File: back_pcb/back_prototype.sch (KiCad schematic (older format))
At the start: 89 parts, among them P1 EXPANSION_LEFT, P2 EXPANSION_BOTTOM, P3 EXPANSION_TOP, P4 USB_A, P5 CONN_01X04, P6 ATMEGA_HEADER, P7 EXPANSION_BOTTOM2, P8 CONN_01X02, Q1 Q_PMOS_GSD, Q2 Q_NMOS_GSD, Q3 Q_NMOS_GSD, U1 PI ZERO, U2 SIM800_BREAKOUT, U3 MCP23017, U4 TP4056_BREAKOUT, U5 RTC, Y1 Crystal_Small

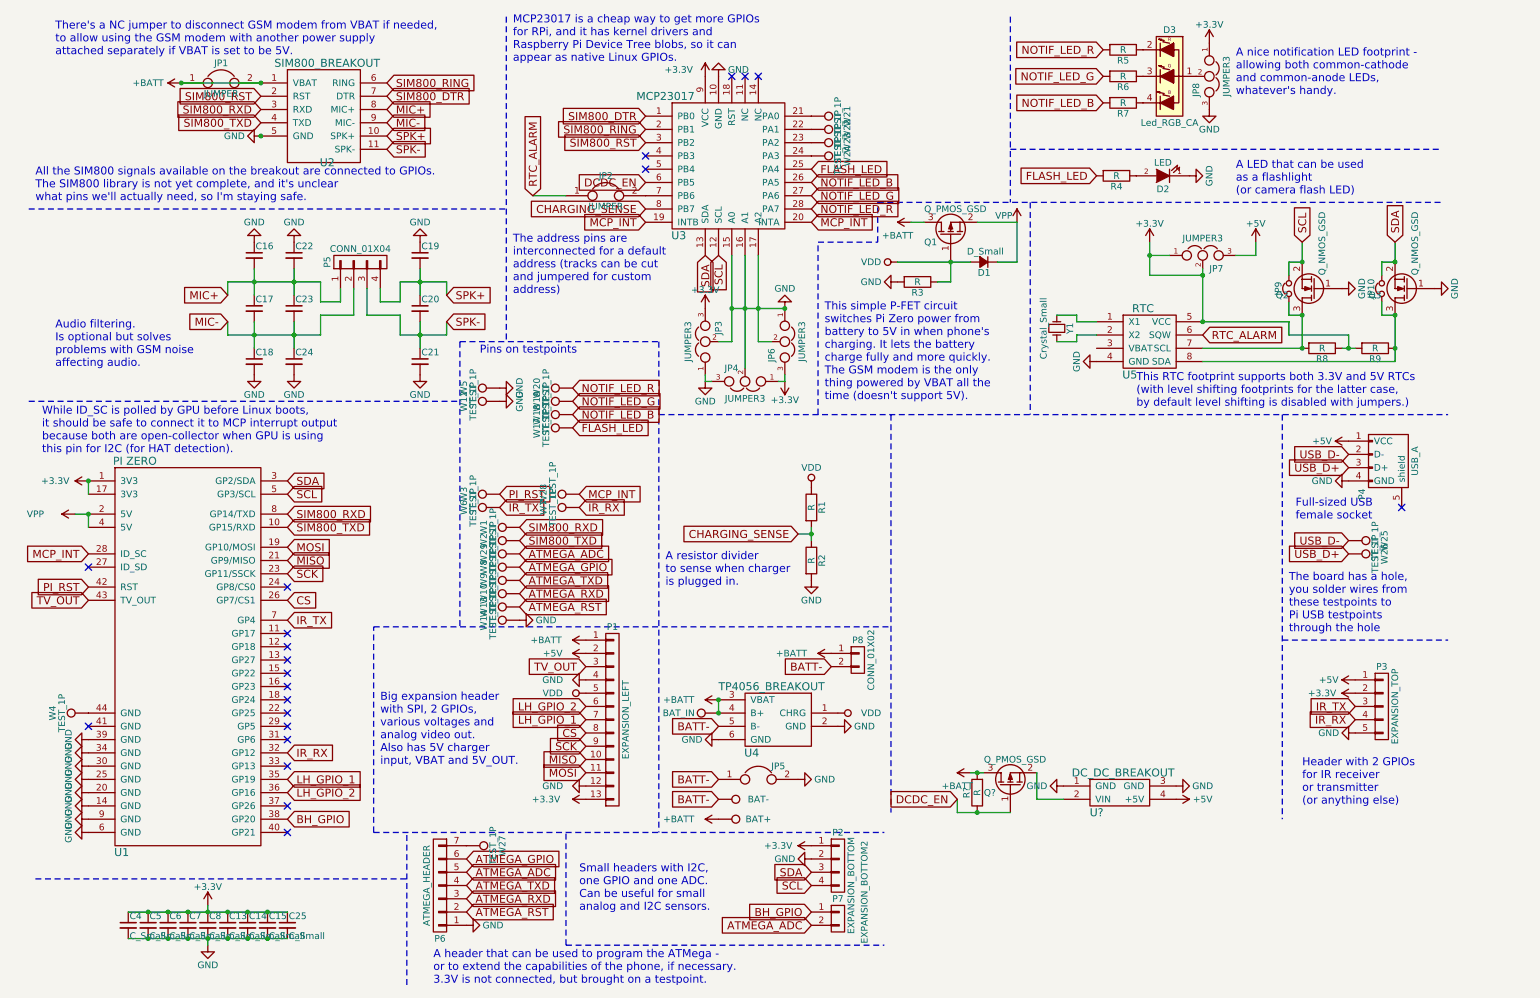
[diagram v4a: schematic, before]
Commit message: Back board finished - untested, not pretty
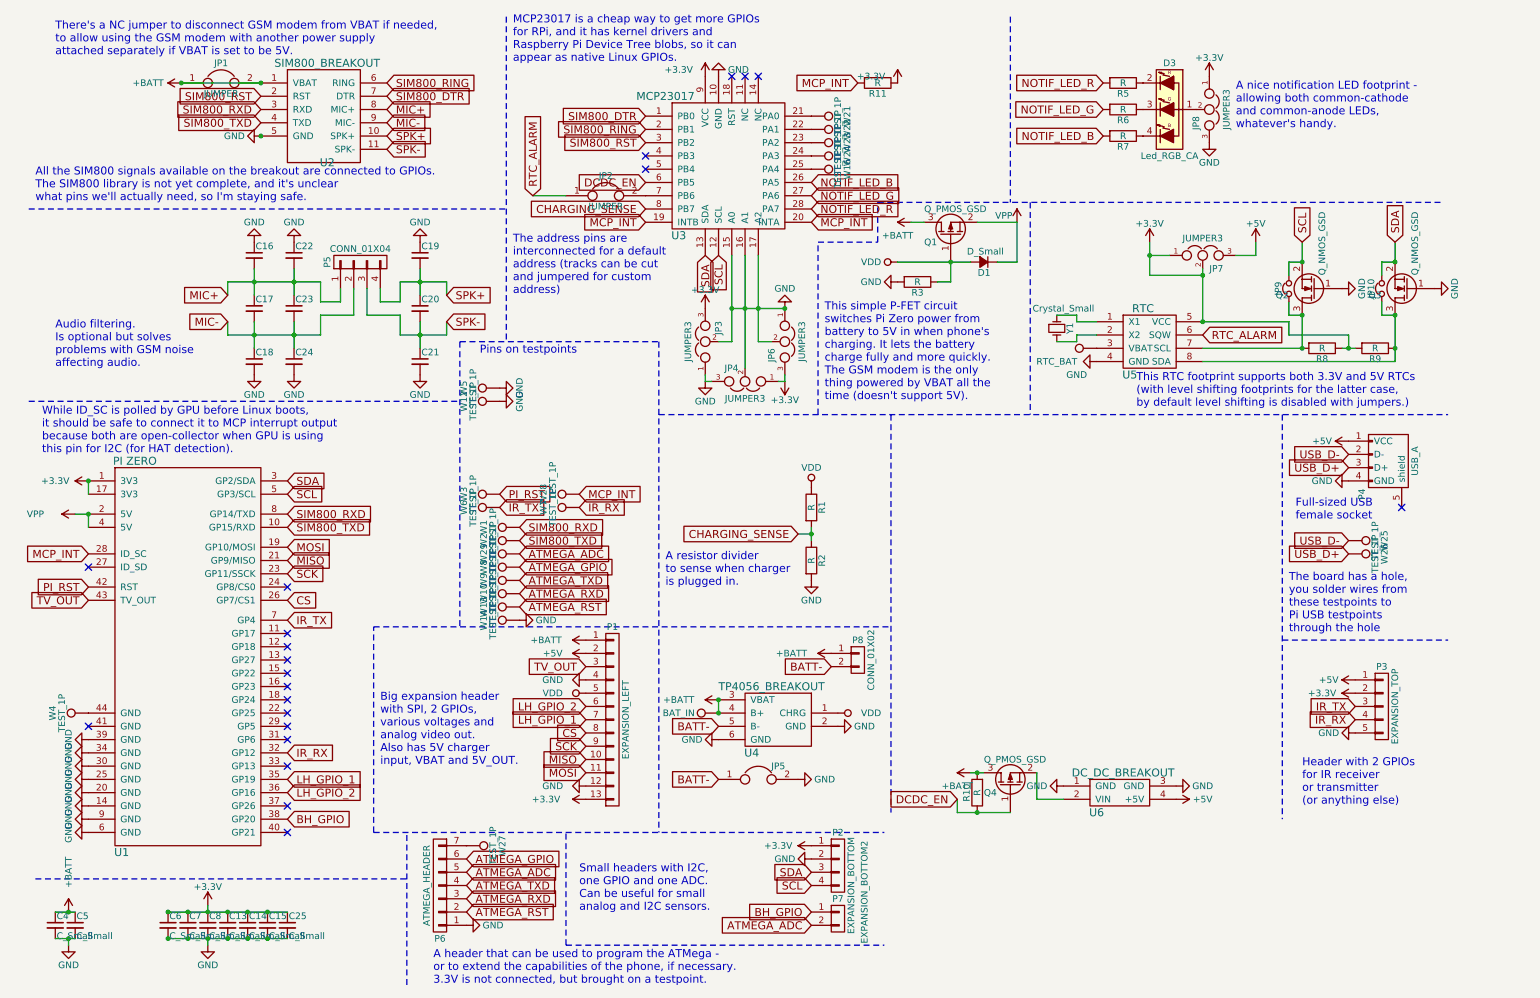
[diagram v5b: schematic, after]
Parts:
- removed D2: LED, symbol LED
- removed R4: R, Resistors_SMD:R_0805_HandSoldering, symbol R
- removed W17, W18, W19, W20: TEST_1P, Measurement_Points:Measurement_Point_Square-SMD-Pad_Small, symbol TEST_1P
- added R11: R, Resistors_SMD:R_0805_HandSoldering, symbol R
- C4: footprint Capacitors_SMD:C_0805 -> Capacitors_Tantalum_SMD:CP_Tantalum_Case-B_EIA-3528-21_Hand
- D3: footprint (none) -> footprints:RGB_5050
- U6: renamed from U?; footprint (none) -> footprints:DC-DC-BREAKOUT
- W15: value BAT- -> RTC_BAT
- W16: value BAT+ -> TEST_1P
- gave numbers to parts that had none: 2
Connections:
- net +3V3: now also R11.1; no longer C4.1, C5.1
- net +BATT: now also C4.1, C5.1; no longer W16.1
- net BATT-: no longer W15.1
- net MCP_INT: now also R11.2
- net at U5.3 (VBAT): now also W15.1
- net FLASH_LED: no longer names the net of U3.25 (PA4)
- net FLASH_LED: now also W16.1
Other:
- note removed: "A LED that can be used \nas a flashlight \n(or camera flash LED)"
- moved on the sheet: C4, C5, D3, JP8, R5, R6, R7

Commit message: Added component values to the back PCB - for BOM
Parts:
- C13, C14, C15, C25, C5, C6, C7, C8: value C_Small -> 100nF
- C16, C17, C18, C19, C20, C21: value C_Small -> 10pF
- C22, C23, C24: value C_Small -> 33pF
- C4: value C_Small -> 10uF
- D1: value D_Small -> SS14
- D3: value Led_RGB_CA -> Led_RGB_CA_CC
- JP3: value JUMPER3 -> A0
- JP4: value JUMPER3 -> A1
- JP6: value JUMPER3 -> A2
- JP7: value JUMPER3 -> 3V3/5V
- JP8: value JUMPER3 -> CA/CC
- P5: value CONN_01X04 -> AUDIO_CONN
- Q1, Q4: value Q_PMOS_GSD -> IRLML6401
- Q2, Q3: value Q_NMOS_GSD -> BSS138
- R1, R10, R11, R2, R3, R8, R9: value R -> 10K
- R5, R6, R7: value R -> 1K
- Y1: value Crystal_Small -> 32.768Hz

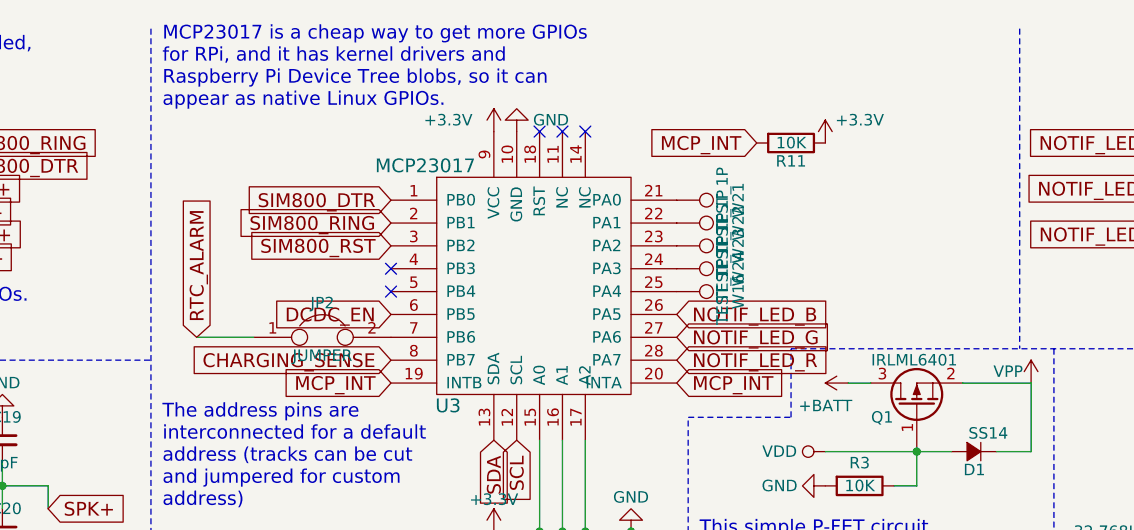
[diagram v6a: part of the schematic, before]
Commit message: MCP RESET pin connected to 3V3, moved some symbols so that schematic is more clear
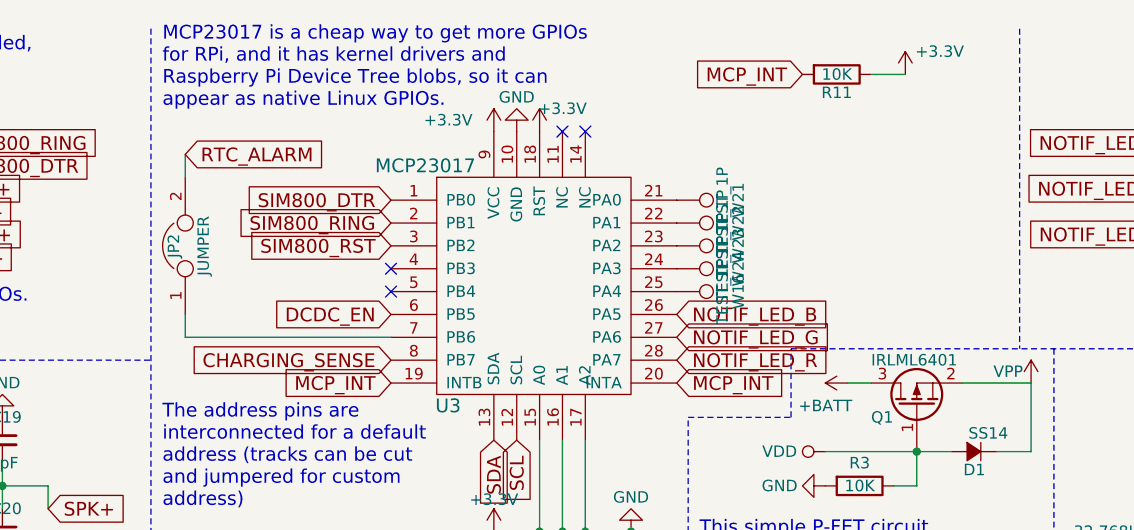
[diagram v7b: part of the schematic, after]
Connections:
- net +3V3: now also U3.18 (RST)
- net RTC_ALARM: now also JP2.2; no longer JP2.1
- net at U3.7 (PB6): now also JP2.1; no longer JP2.2
- no-connect marks 21 -> 20
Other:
- moved on the sheet: JP2, R11
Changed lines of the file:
@@
 P 5700 950
 F 0 "#PWR025" H 5700 700 50  0001 C CNN
-F 1 "GND" H 5550 900 50  0000 C CNN
+F 1 "GND" H 5700 800 50  0000 C CNN
 F 2 "" H 5700 950 50  0000 C CNN
 F 3 "" H 5700 950 50  0000 C CNN
@@
 	-1   0    0    1
 $EndComp
-NoConn ~ 5800 950
 NoConn ~ 5900 950
 NoConn ~ 6000 950
@@
 Text GLabel 9350 2900 2    60   Input ~ 0
 RTC_ALARM
-Text GLabel 4300 1850 1    60   Input ~ 0
+Text GLabel 4250 1050 2    60   Input ~ 0
 RTC_ALARM
 $Comp
@@
 L JUMPER JP2
 U 1 1 588B1D7A
-P 4850 1850
-F 0 "JP2" H 4850 2000 50  0000 C CNN
-F 1 "JUMPER" H 4850 1770 50  0000 C CNN
-F 2 "Connect:GS2" H 4850 1850 50  0001 C CNN
-F 3 "" H 4850 1850 50  0000 C CNN
-	1    4850 1850
-	1    0    0    -1
+P 4250 1450
+F 0 "JP2" H 4250 1500 50  0000 C CNN
+F 1 "JUMPER" H 4250 1370 50  0000 C CNN
+F 2 "Connect:GS2" H 4250 1450 50  0001 C CNN
+F 3 "" H 4250 1450 50  0000 C CNN
+	1    4250 1450
+	0    -1   -1   0
 $EndComp
 Text Notes 700  800  0    60   ~ 0
@@
 	7450 2500 7450 2350
 Wire Wire Line
-	4300 1850 4550 1850
-Wire Wire Line
 	950  4100 950  4000
 Connection ~ 950  4000
@@
 	700  7250 850  7250
 Connection ~ 800  7250
-Text GLabel 6750 1000 0    60   Input ~ 0
+Text GLabel 6950 700  0    60   Input ~ 0
 MCP_INT
 $Comp
 L R R11
 U 1 1 58914037
-P 6900 1000
-F 0 "R11" V 6980 1000 50  0000 C CNN
-F 1 "10K" V 6900 1000 50  0000 C CNN
-F 2 "Resistors_SMD:R_0805_HandSoldering" V 6830 1000 50  0001 C CNN
-F 3 "" H 6900 1000 50  0000 C CNN
-	1    6900 1000
+P 7100 700
+F 0 "R11" V 7180 700 50  0000 C CNN
+F 1 "10K" V 7100 700 50  0000 C CNN
+F 2 "Resistors_SMD:R_0805_HandSoldering" V 7030 700 50  0001 C CNN
+F 3 "" H 7100 700 50  0000 C CNN
+	1    7100 700
 	0    1    1    0
 $EndComp
@@
 L +3.3V #PWR068
 U 1 1 58914166
-P 7050 1000
-F 0 "#PWR068" H 7050 850 50  0001 C CNN
-F 1 "+3.3V" H 7200 1100 50  0000 C CNN
-F 2 "" H 7050 1000 50  0000 C CNN
-F 3 "" H 7050 1000 50  0000 C CNN
-	1    7050 1000
+P 7400 700
+F 0 "#PWR068" H 7400 550 50  0001 C CNN
+F 1 "+3.3V" H 7550 800 50  0000 C CNN
+F 2 "" H 7400 700 50  0000 C CNN
+F 3 "" H 7400 700 50  0000 C CNN
+	1    7400 700
 	1    0    0    -1
 $EndComp
@@
 	1    0    0    -1
 $EndComp
+$Comp
+L +3.3V #PWR?
+U 1 1 58BD09E1
+P 5800 950
+F 0 "#PWR?" H 5800 800 50  0001 C CNN
+F 1 "+3.3V" H 5900 1050 50  0000 C CNN
+F 2 "" H 5800 950 50  0000 C CNN
+F 3 "" H 5800 950 50  0000 C CNN
+	1    5800 950
+	1    0    0    -1
+$EndComp
+Wire Wire Line
+	4250 1150 4250 1050
+Wire Wire Line
+	4250 1750 4250 1850
+Wire Wire Line
+	4250 1850 5150 1850
+Wire Wire Line
+	7250 700  7400 700
 $EndSCHEMATC
